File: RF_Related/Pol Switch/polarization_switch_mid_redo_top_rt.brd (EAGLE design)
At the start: 88.4 x 54.4 mm, 53 parts, among them IC1 VLPR-24-858-2, IC10 ADP-2-1+_MINICIRCUITS, IC11 ADP-2-1+_MINICIRCUITS, IC12 QCV-151+, IC13 MAX8878EUK28+T, IC14 SN74LVC2G17DBVT, IC15 SN74LVC2G17DBVT, IC2 VLPR-24-858-2, IC3 HSWA2-30DR+, IC4 VLPR-24-858-2, IC5 HSWA2-30DR+, IC6 HSWA2-30DR+, IC7 HSWA2-30DR+, IC8 PHA-13LN+, IC9 PHA-13LN+, J1 M20-9730645, J2 171856-0002, X1 SMA-142-0701-801/806, X2 SMA-142-0701-801/806, X3 SMA-142-0701-801/806

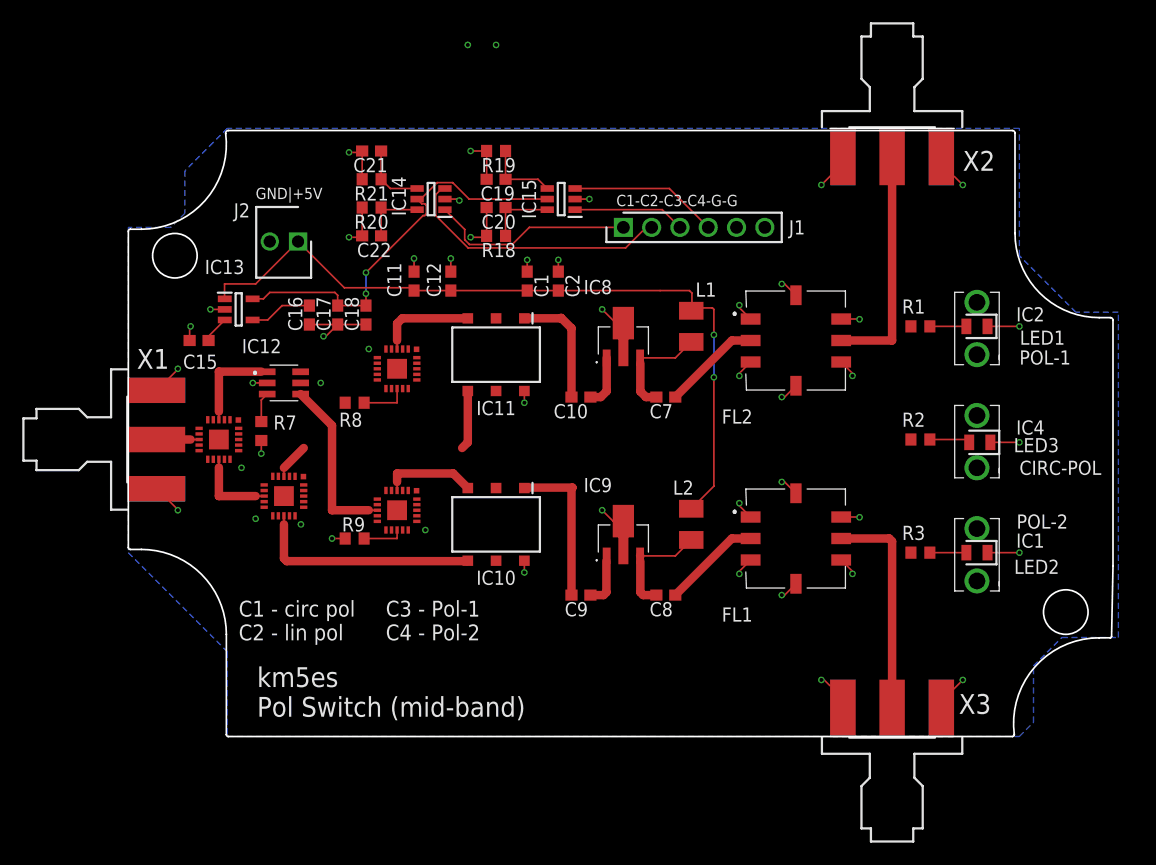
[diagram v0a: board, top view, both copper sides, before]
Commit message: made a new version of the pol switch. already sent to OSH park for fab. note that there is a template for routing as well as a completed circuit
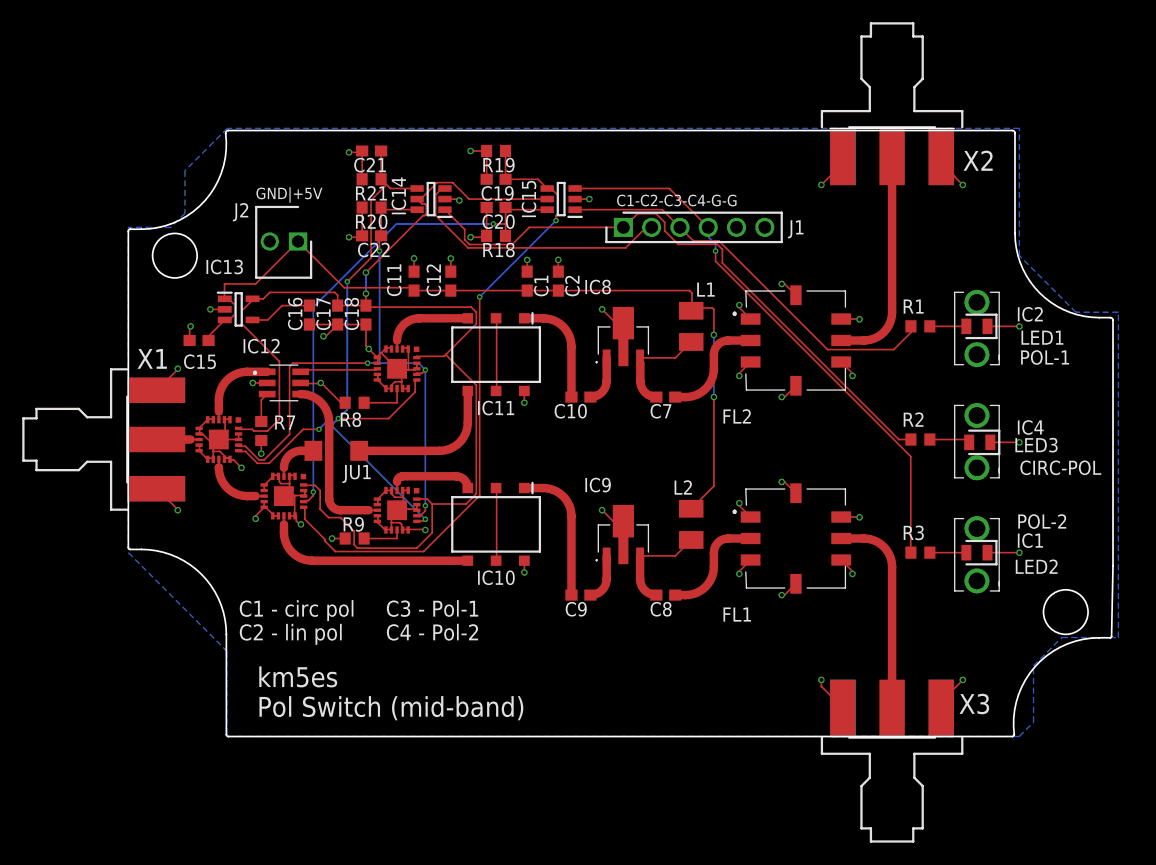
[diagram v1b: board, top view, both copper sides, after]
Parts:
- added JU1: (no value), rcl_jumper_pads:R1206
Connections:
- new net N$10: IC11.4, JU1.2
- net N$12: now also JU1.1; no longer IC11.4
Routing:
- net GND: track 82.3 -> 168.4 mm, vias 49 -> 47
- net N$39: track 36.8 -> 109.8 mm
- net N$46: track 6.14 -> 62.8 mm, vias 0 -> 4
- net N$38: track 6.62 -> 58.0 mm, vias 0 -> 2
- net N$42: track 5.86 -> 56.8 mm, vias 0 -> 4
- net N$8: track 6.25 -> 44.6 mm, vias 0 -> 2
- net N$45: track 13.4 -> 50.2 mm, vias 0 -> 1
- net N$37: track 18.5 -> 54.4 mm
- net N$44: track 10.1 -> 36.5 mm
- net N$10: track 0.00 -> 13.6 mm
- net N$16: track 0.00 -> 6.99 mm
- net N$22: track 0.00 -> 6.56 mm
- net N$25: track 0.00 -> 6.56 mm
- net N$12: track 8.61 -> 4.04 mm
- net N$36: track 71.8 -> 74.9 mm
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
